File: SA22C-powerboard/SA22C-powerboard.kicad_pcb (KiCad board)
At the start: 2 copper layers, 45 x 65 mm, 22 parts, among them J1 Barrel_Jack_MountingPin, J4 Conn_01x09_Pin, J5 Conn_01x09_Pin, J6 Conn_01x02_Pin, J7 Conn_02x09_Odd_Even_MountingP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, U1 LM7805_TO220

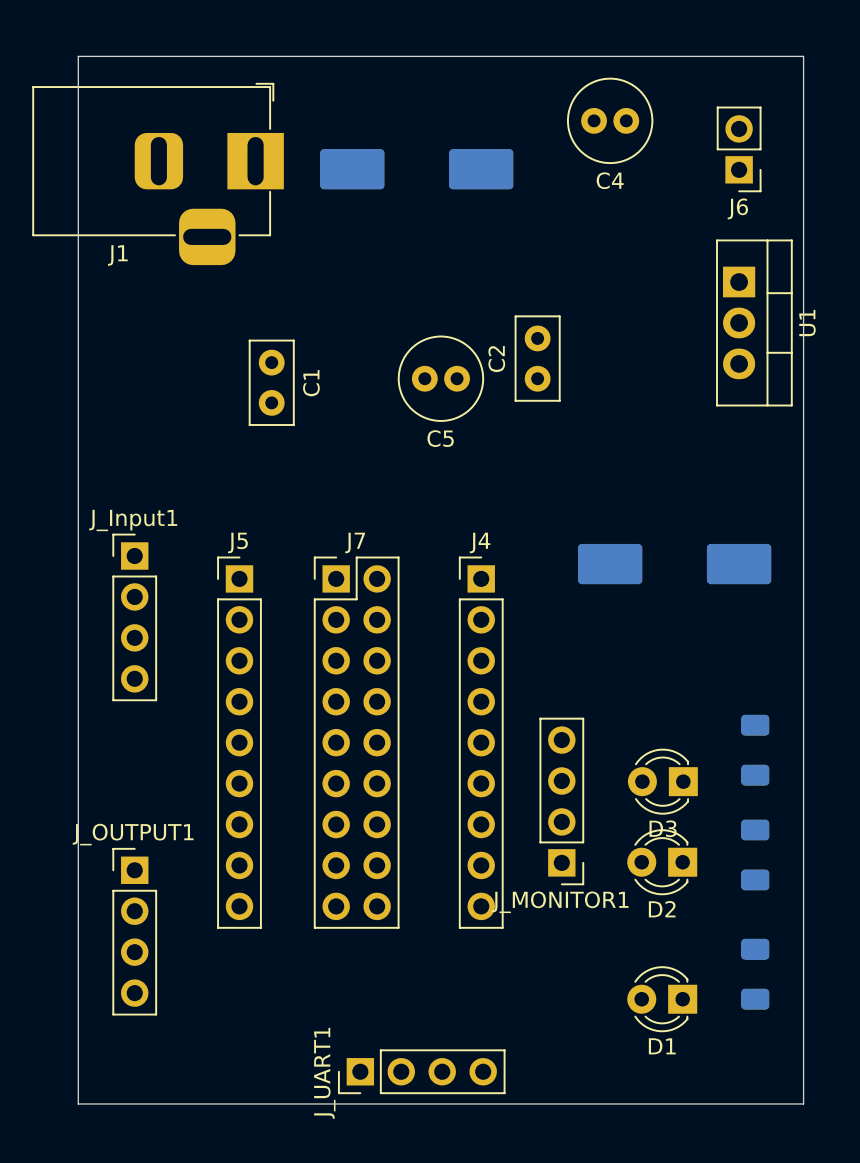
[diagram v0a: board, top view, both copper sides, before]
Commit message: Placement drafted, now on to gnd plane and cleanup/simplification
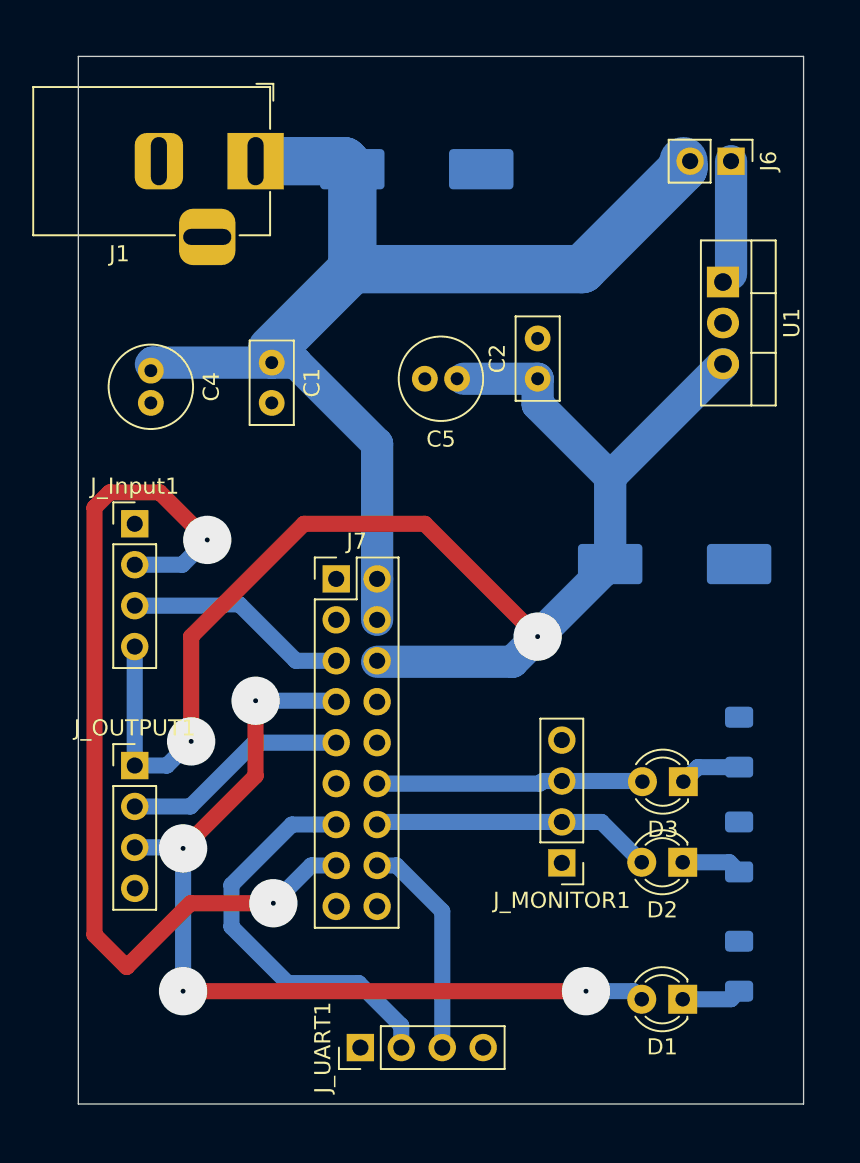
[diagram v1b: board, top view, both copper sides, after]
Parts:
- removed J4, J5: Conn_01x09_Pin, Connector_PinHeader_2.54mm:PinHeader_1x09_P2.54mm_Vertical
- moved C4 33.3 mm to (104.5, 70.5), turned to -90 degrees
- moved J_OUTPUT1 6.50 mm to (103.5, 95.0)
- moved J_Input1 2.00 mm to (103.5, 80.0)
- moved J_UART1 1.50 mm to (117.5, 112.5)
- moved R1 1.12 mm to (141.0, 107.5)
- moved R2 1.12 mm to (141.0, 100.0)
- moved R3 1.12 mm to (141.0, 93.5), turned to 90 degrees
- moved U1 1.00 mm to (140.0, 65.0)
- moved J6 0.74 mm to (140.5, 57.5), turned to -90 degrees
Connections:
- J7 pad 17: Net-(J5-Pin_9) -> unconnected-(J7-Pin_17-Pad17)
- J7 pad 18: Net-(J4-Pin_9) -> unconnected-(J7-Pin_18-Pad18)
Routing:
- net +5V: track 0.00 -> 90.1 mm, vias 0 -> 2
- net +15V: track 0.00 -> 70.1 mm
- net /PPS_IN: track 0.00 -> 58.7 mm, vias 0 -> 2
- net /PPS_OUT: track 0.00 -> 56.6 mm, vias 0 -> 4
- net /UART_DIN: track 0.00 -> 25.1 mm
- net /LOCK: track 0.00 -> 17.5 mm
- net /SERVICE: track 0.00 -> 16.5 mm
- net /FACMOS: track 0.00 -> 14.1 mm
- net /FREQCTL: track 0.00 -> 14.0 mm
- net /UART_DOUT: track 0.00 -> 13.7 mm
- net Net-(J6-Pin_1): track 0.00 -> 7.71 mm
- net Net-(D3-K): track 0.00 -> 3.83 mm
- net Net-(D2-K): track 0.00 -> 3.75 mm
- net Net-(D1-K): track 0.00 -> 3.71 mm

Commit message: GND plane ok ish, making it easier for hand soldering
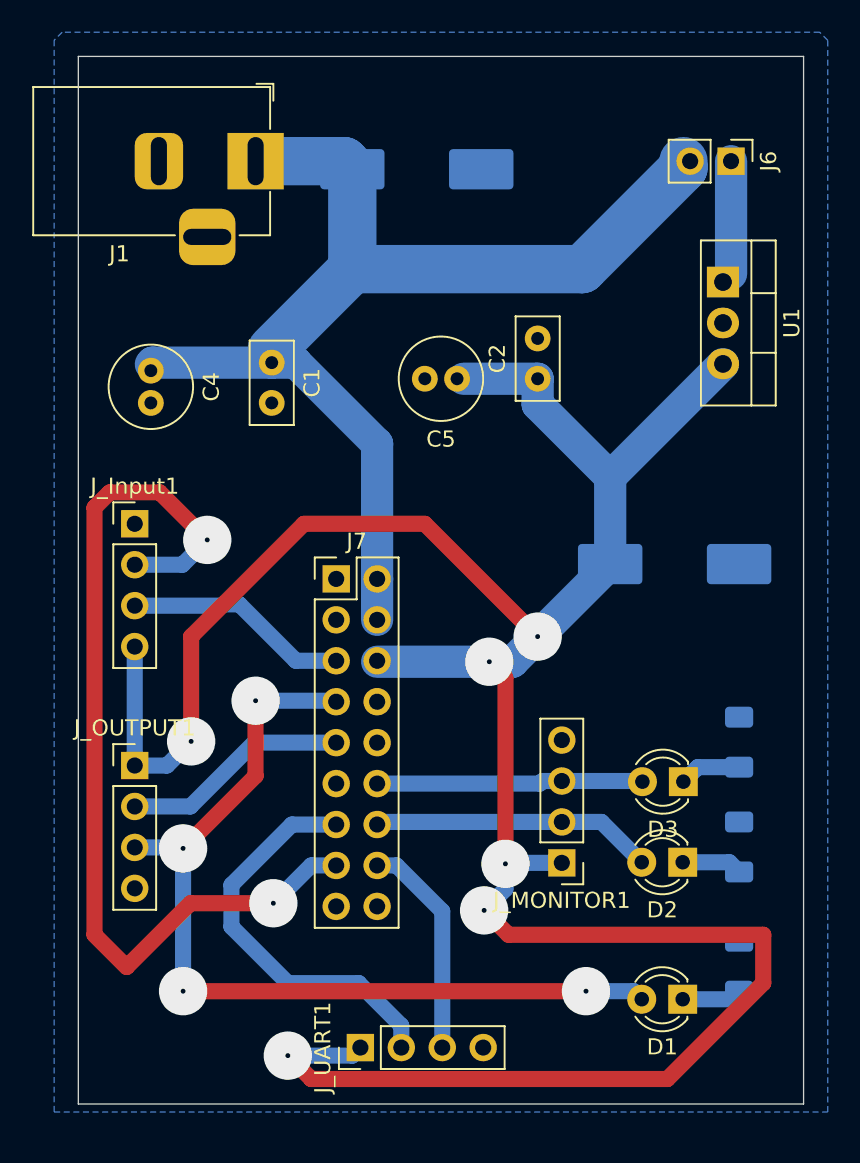
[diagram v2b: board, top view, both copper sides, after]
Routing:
- net +5V: track 90.1 -> 168.3 mm, vias 2 -> 6
- added copper zone on B.Cu, net GND
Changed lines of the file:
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@@
+	)
+	(segment
+		(start 125.179494 103.98658)
+		(end 126.692914 105.5)
+		(width 1)
+		(layer "F.Cu")
+		(net 3)
+	)
+	(segment
+		(start 126.5 101.1)
+		(end 126.5 89.56)
+		(width 1)
+		(layer "F.Cu")
+		(net 3)
 	)
 	(segment
@@
 	)
 	(segment
+		(start 142.5 105.5)
+		(end 142.5 108.5)
+		(width 1)
+		(layer "F.Cu")
+		(net 3)
+	)
+	(segment
+		(start 114.45 114.45)
+		(end 113 113)
+		(width 1)
+		(layer "F.Cu")
+		(net 3)
+	)
+	(segment
+		(start 136.55 114.45)
+		(end 114.45 114.45)
+		(width 1)
+		(layer "F.Cu")
+		(net 3)
+	)
+	(segment
 		(start 121.5 80)
 		(end 128.5 87)
@@
 	)
 	(segment
+		(start 126.5 89.56)
+		(end 125.5 88.56)
+		(width 1)
+		(layer "F.Cu")
+		(net 3)
+	)
+	(segment
 		(start 107 93.5)
 		(end 107 87)
@@
 		(net 3)
 	)
+	(segment
+		(start 126.692914 105.5)
+		(end 142.5 105.5)
+		(width 1)
+		(layer "F.Cu")
+		(net 3)
+	)
+	(segment
+		(start 142.5 108.5)
+		(end 136.55 114.45)
+		(width 1)
+		(layer "F.Cu")
+		(net 3)
+	)
+	(via
+		(at 126.5 101.1)
+		(size 3)
+		(drill 0.3)
+		(layers "F.Cu" "B.Cu")
+		(net 3)
+	)
 	(via
 		(at 128.5 87)
@@
 	)
 	(via
+		(at 125.179494 103.98658)
+		(size 3)
+		(drill 0.3)
+		(layers "F.Cu" "B.Cu")
+		(net 3)
+	)
+	(via
+		(at 125.5 88.56)
+		(size 3)
+		(drill 0.3)
+		(layers "F.Cu" "B.Cu")
+		(net 3)
+	)
+	(via
+		(at 113 113)
+		(size 3)
+		(drill 0.3)
+		(layers "F.Cu" "B.Cu")
+		(net 3)
+	)
+	(via
 		(at 107 93.5)
 		(size 3)
 		(drill 0.3)
 		(layers "F.Cu" "B.Cu")
-		(net 3)
-	)
-	(segment
-		(start 126.94 88.56)
-		(end 118.54 88.56)
-		(width 2)
-		(layer "B.Cu")
 		(net 3)
 	)
@@
 	)
 	(segment
+		(start 126.5 102.666074)
+		(end 125.179494 103.98658)
+		(width 1)
+		(layer "B.Cu")
+		(net 3)
+	)
+	(segment
 		(start 103.5 95)
 		(end 105.5 95)
@@
 	)
 	(segment
+		(start 125.5 88.56)
+		(end 118.54 88.56)
+		(width 2)
+		(layer "B.Cu")
+		(net 3)
+	)
+	(segment
+		(start 130 101.04)
+		(end 126.56 101.04)
+		(width 1)
+		(layer "B.Cu")
+		(net 3)
+	)
+	(segment
+		(start 126.56 101.04)
+		(end 126.5 101.1)
+		(width 1)
+		(layer "B.Cu")
+		(net 3)
+	)
+	(segment
+		(start 113 113)
+		(end 117 113)
+		(width 1)
+		(layer "B.Cu")
+		(net 3)
+	)
+	(segment
 		(start 128.5 71)
 		(end 123.9 71)
@@
 	)
 	(segment
+		(start 126.5 101.1)
+		(end 126.5 102.666074)
+		(width 1)
+		(layer "B.Cu")
+		(net 3)
+	)
+	(segment
+		(start 117 113)
+		(end 117.5 112.5)
+		(width 1)
+		(layer "B.Cu")
+		(net 3)
+	)
+	(segment
+		(start 126.94 88.56)
+		(end 125.5 88.56)
+		(width 2)
+		(layer "B.Cu")
+		(net 3)
+	)
+	(segment
 		(start 133 77.0925)
 		(end 140 70.0925)
@@
 		(net 15)
 	)
+	(zone
+		(net 1)
+		(net_name "GND")
+		(layer "B.Cu")
+		(hatch edge 0.5)
+		(connect_pads yes
+			(clearance 0.5)
+		)
+		(min_thickness 0.25)
+		(filled_areas_thickness no)
+		(fill yes
+			(thermal_gap 0.5)
+			(thermal_bridge_width 0.5)
+		)
+		(polygon
+			(pts
+				(xy 146.5 116.5) (xy 146.5 50) (xy 146 49.5) (xy 99 49.5) (xy 98.5 50) (xy 98.5 116.5)
+			)
+		)
+	)
 )

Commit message: Looks ready for home production
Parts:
- renumbered D2 to D_LOCK, D1 to D_PPS_OUT, D3 to D_SERVICE
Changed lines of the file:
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@@
 			(at -6.2 -5.5 0)
 			(layer "F.Fab")
+			(hide yes)
 			(effects
 				(font
@@
 			(at 1 3.75 180)
 			(layer "F.Fab")
+			(hide yes)
 			(effects
 				(font
@@
 			(at 0 4.87 90)
 			(layer "F.Fab")
+			(hide yes)
 			(effects
 				(font
@@
 		(tags "Through hole pin header THT 1x04 2.54mm single row")
 		(property "Reference" "J_OUTPUT1"
-			(at 0 -2.33 0)
+			(at -1 14 90)
 			(layer "F.SilkS")
 			(effects
@@
 			(at 0 9.95 0)
 			(layer "F.Fab")
+			(hide yes)
 			(effects
 				(font
@@
 		(tags "Through hole pin header THT 1x04 2.54mm single row")
 		(property "Reference" "J_Input1"
-			(at 0 -2.33 0)
+			(at 1 -3 0)
 			(layer "F.SilkS")
 			(effects
@@
 			(at 0 9.95 0)
 			(layer "F.Fab")
+			(hide yes)
 			(effects
 				(font
@@
 		(descr "LED, diameter 3.0mm, 2 pins")
 		(tags "LED diameter 3.0mm 2 pins")
-		(property "Reference" "D3"
-			(at 1.27 -2.96 180)
+		(property "Reference" "D_SERVICE"
+			(at 0.04 3 180)
 			(layer "F.SilkS")
 			(effects
@@
 			(at 1.27 2.96 180)
 			(layer "F.Fab")
+			(hide yes)
 			(effects
 				(font
@@
 		(descr "LED, diameter 3.0mm, 2 pins")
 		(tags "LED diameter 3.0mm 2 pins")
-		(property "Reference" "D2"
+		(property "Reference" "D_LOCK"
 			(at 1.27 -2.96 180)
 			(layer "F.SilkS")
@@
 			(at 1.27 2.96 180)
 			(layer "F.Fab")
+			(hide yes)
 			(effects
 				(font
@@
 			(at 1.27 22.65 0)
 			(layer "F.Fab")
+			(hide yes)
 			(effects
 				(font
@@
 		(descr "LED, diameter 3.0mm, 2 pins")
 		(tags "LED diameter 3.0mm 2 pins")
-		(property "Reference" "D1"
+		(property "Reference" "D_PPS_OUT"
 			(at 1.27 -2.96 180)
 			(layer "F.SilkS")
@@
 			(at 1.27 2.96 180)
 			(layer "F.Fab")
+			(hide yes)
 			(effects
 				(font
@@
 			(at 1.25 2.5 270)
 			(layer "F.Fab")
+			(hide yes)
 			(effects
 				(font
@@
 			(at 1.25 2.5 90)
 			(layer "F.Fab")
+			(hide yes)
 			(effects
 				(font
@@
 		(tags "Through hole pin header THT 1x04 2.54mm single row")
 		(property "Reference" "J_MONITOR1"
-			(at 0 -2.33 180)
+			(at -2.5 3.54 -90)
 			(layer "F.SilkS")
 			(effects
@@
 			(at 0 9.95 180)
 			(layer "F.Fab")
+			(hide yes)
 			(effects
 				(font
@@
 			(at 1 3.75 90)
 			(layer "F.Fab")
+			(hide yes)
 			(effects
 				(font
@@
 		(tags "Through hole pin header THT 1x04 2.54mm single row")
 		(property "Reference" "J_UART1"
-			(at 0 -2.33 270)
+			(at 2.5 4.5 180)
 			(layer "F.SilkS")
 			(effects
@@
 			(at 0 9.95 270)
 			(layer "F.Fab")
+			(hide yes)
 			(effects
 				(font
@@
 	)
 	(gr_rect
+		(start 113.5 81)
+		(end 117.27 84.77)
+		(stroke
+			(width 0.1)
+			(type solid)
+		)
+		(fill solid)
+		(layer "F.SilkS")
+	)
+	(gr_rect
 		(start 100 51)
 		(end 145 116)
@@
 		(start 137.55 57.91)
 		(end 137.55 57.5)
-		(width 3)
+		(width 2)
 		(layer "B.Cu")
 		(net 2)
@@
 		(start 131.26 64.2)
 		(end 137.55 57.91)
-		(width 3)
+		(width 2)
 		(layer "B.Cu")
 		(net 2)
@@
 	)
 	(segment
+		(start 126.692914 105.5)
+		(end 125.179494 103.98658)
+		(width 1)
+		(layer "F.Cu")
+		(net 3)
+	)
+	(segment
 		(start 114 80)
 		(end 121.5 80)
@@
 	)
 	(segment
-		(start 125.179494 103.98658)
-		(end 126.692914 105.5)
+		(start 136.55 114.45)
+		(end 142.5 108.5)
 		(width 1)
 		(layer "F.Cu")
@@
 	)
 	(segment
-		(start 142.5 105.5)
-		(end 142.5 108.5)
-		(width 1)
-		(layer "F.Cu")
-		(net 3)
-	)
-	(segment
-		(start 114.45 114.45)
-		(end 113 113)
+		(start 142.5 108.5)
+		(end 142.5 105.5)
 		(width 1)
 		(layer "F.Cu")
@@
 	)
 	(segment
-		(start 136.55 114.45)
+		(start 113.671519 111.601292)
 		(end 114.45 114.45)
 		(width 1)
@@
 	)
 	(segment
-		(start 121.5 80)
-		(end 128.5 87)
+		(start 142.5 105.5)
+		(end 126.692914 105.5)
 		(width 1)
 		(layer "F.Cu")
@@
 	)
 	(segment
-		(start 126.5 89.56)
-		(end 125.5 88.56)
+		(start 114.45 114.45)
+		(end 136.55 114.45)
 		(width 1)
 		(layer "F.Cu")
@@
 	)
 	(segment
-		(start 107 93.5)
-		(end 107 87)
+		(start 121.5 80)
+		(end 128.5 87)
 		(width 1)
 		(layer "F.Cu")
@@
 	)
 	(segment
-		(start 126.692914 105.5)
-		(end 142.5 105.5)
+		(start 126.5 89.56)
+		(end 125.5 88.56)
 		(width 1)
 		(layer "F.Cu")
@@
 	)
 	(segment
-		(start 142.5 108.5)
-		(end 136.55 114.45)
+		(start 107 93.5)
+		(end 107 87)
 		(width 1)
 		(layer "F.Cu")
@@
 	)
 	(via
-		(at 113 113)
+		(at 113.671519 111.601292)
 		(size 3)
 		(drill 0.3)
@@
 	)
 	(segment
-		(start 113 113)
-		(end 117 113)
+		(start 116.601292 111.601292)
+		(end 117.5 112.5)
 		(width 1)
 		(layer "B.Cu")
@@
 	)
 	(segment
+		(start 113.671519 111.601292)
+		(end 116.601292 111.601292)
+		(width 1)
+		(layer "B.Cu")
+		(net 3)
+	)
+	(segment
 		(start 103.5 87.62)
 		(end 103.5 95)
@@
 	)
 	(segment
-		(start 117 113)
-		(end 117.5 112.5)
-		(width 1)
-		(layer "B.Cu")
-		(net 3)
-	)
-	(segment
 		(start 126.94 88.56)
 		(end 125.5 88.56)
@@
 	)
 	(zone
+		(net 0)
+		(net_name "")
+		(layer "B.Cu")
+		(hatch edge 0.5)
+		(connect_pads yes
+			(clearance 0)
+		)
+		(min_thickness 0.25)
+		(filled_areas_thickness no)
+		(keepout
+			(tracks allowed)
+			(vias allowed)
+			(pads allowed)
+			(copperpour not_allowed)
+			(footprints allowed)
+		)
+		(fill
+			(thermal_gap 0.5)
+			(thermal_bridge_width 0.5)
+		)
+		(polygon
+			(pts
+				(xy 139.5 92.5) (xy 139.5 94.5) (xy 140 95) (xy 142 95) (xy 142.5 94.5) (xy 142.5 92.5)
+			)
+		)
+	)
+	(zone
+		(net 0)
+		(net_name "")
+		(layer "B.Cu")
+		(hatch edge 0.5)
+		(connect_pads yes
+			(clearance 0)
+		)
+		(min_thickness 0.25)
+		(filled_areas_thickness no)
+		(keepout
+			(tracks allowed)
+			(vias allowed)
+			(pads allowed)
+			(copperpour not_allowed)
+			(footprints allowed)
+		)
+		(fill
+			(thermal_gap 0.5)
+			(thermal_bridge_width 0.5)
+		)
+		(polygon
+			(pts
+				(xy 133 78) (xy 139.5 78) (xy 139.5 86.5) (xy 138.5 87.5) (xy 131.5 87.5) (xy 131.5 79.5)
+			)
+		)
+	)
+	(zone
 		(net 1)
 		(net_name "GND")
@@
 			)
 		)
+	)
+	(zone
+		(net 0)
+		(net_name "")
+		(layer "B.Cu")
+		(hatch edge 0.5)
+		(connect_pads yes
+			(clearance 0)
+		)
+		(min_thickness 0.25)
+		(filled_areas_thickness no)
+		(keepout
+			(tracks allowed)
+			(vias allowed)
+			(pads allowed)
+			(copperpour not_allowed)
+			(footprints allowed)
+		)
+		(fill
+			(thermal_gap 0.5)
+			(thermal_bridge_width 0.5)
+		)
+		(polygon
+			(pts
+				(xy 139.5 106.5) (xy 142 106.5) (xy 142.5 107) (xy 142.5 108.5) (xy 139.5 108.5)
+			)
+		)
+	)
+	(zone
+		(net 0)
+		(net_name "")
+		(layer "B.Cu")
+		(hatch edge 0.5)
+		(connect_pads yes
+			(clearance 0)
+		)
+		(min_thickness 0.25)
+		(filled_areas_thickness no)
+		(keepout
+			(tracks allowed)
+			(vias allowed)
+			(pads allowed)
+			(copperpour not_allowed)
+			(footprints allowed)
+		)
+		(fill
+			(thermal_gap 0.5)
+			(thermal_bridge_width 0.5)
+		)
+		(polygon
+			(pts
+				(xy 116 53) (xy 122.5 53) (xy 123.5 54) (xy 123.5 60.5) (xy 123 61) (xy 123 63) (xy 117 63) (xy 116 62)
+			)
+		)
+	)
+	(zone
+		(net 0)
+		(net_name "")
+		(layer "B.Cu")
+		(hatch edge 0.5)
+		(connect_pads yes
+			(clearance 0)
+		)
+		(min_thickness 0.25)
+		(filled_areas_thickness no)
+		(keepout
+			(tracks allowed)
+			(vias allowed)
+			(pads allowed)
+			(copperpour not_allowed)
+			(footprints allowed)
+		)
+		(fill
+			(thermal_gap 0.5)
+			(thermal_bridge_width 0.5)
+		)
+		(polygon
+			(pts
+				(xy 142.5 101) (xy 142.5 99) (xy 139.5 99) (xy 139.5 101.5) (xy 142 101.5)
+			)
+		)
